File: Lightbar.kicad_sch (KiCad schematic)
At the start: 17 parts, among them IC1 PAM2863ECR, IC2 PAM2863ECR, J1 Conn_01x04_Pin

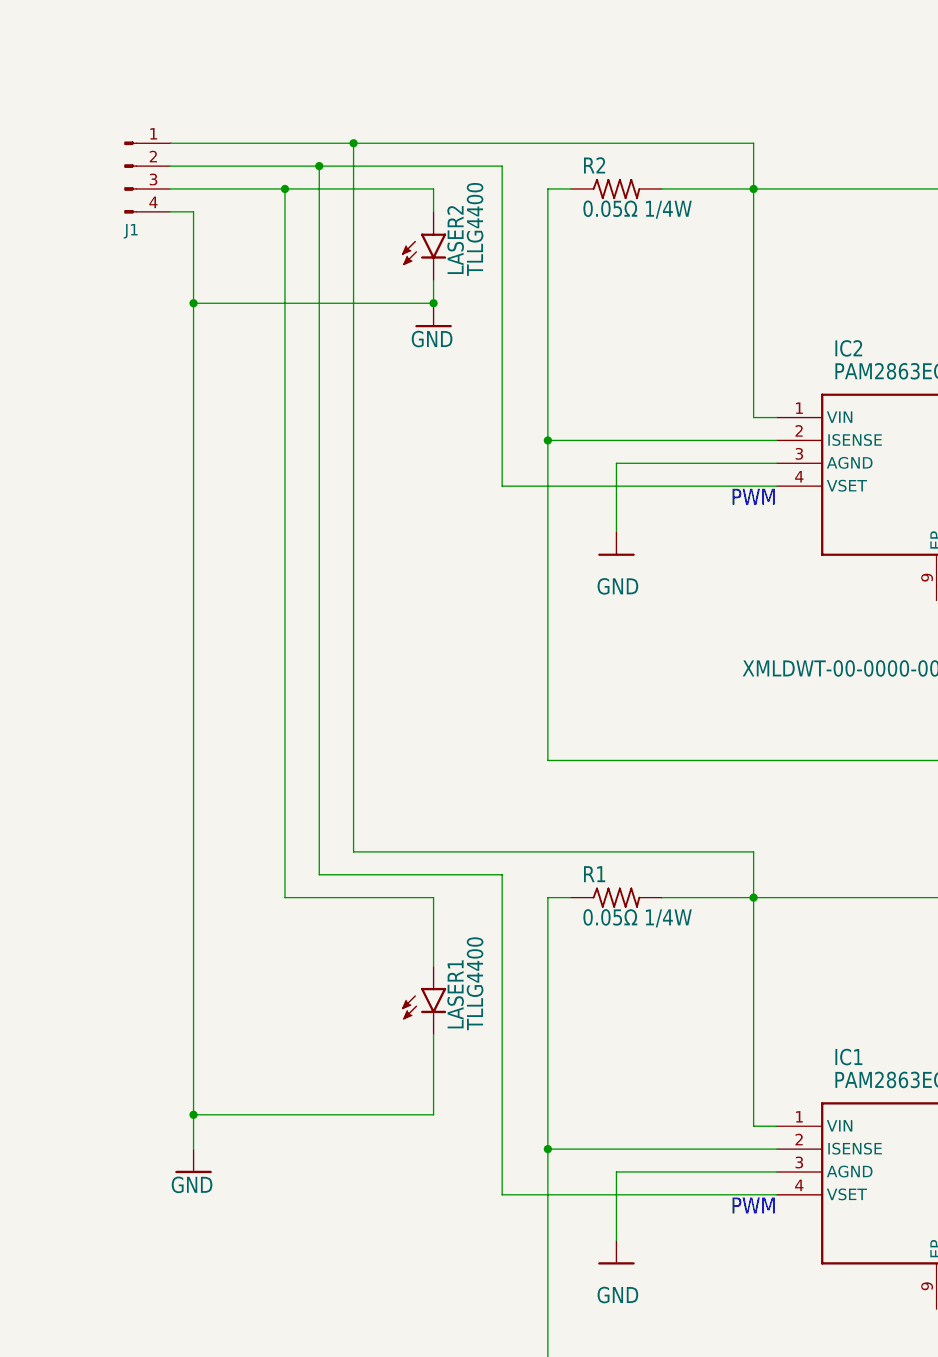
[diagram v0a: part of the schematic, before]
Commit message: updated lightbar
added resistors and transistor
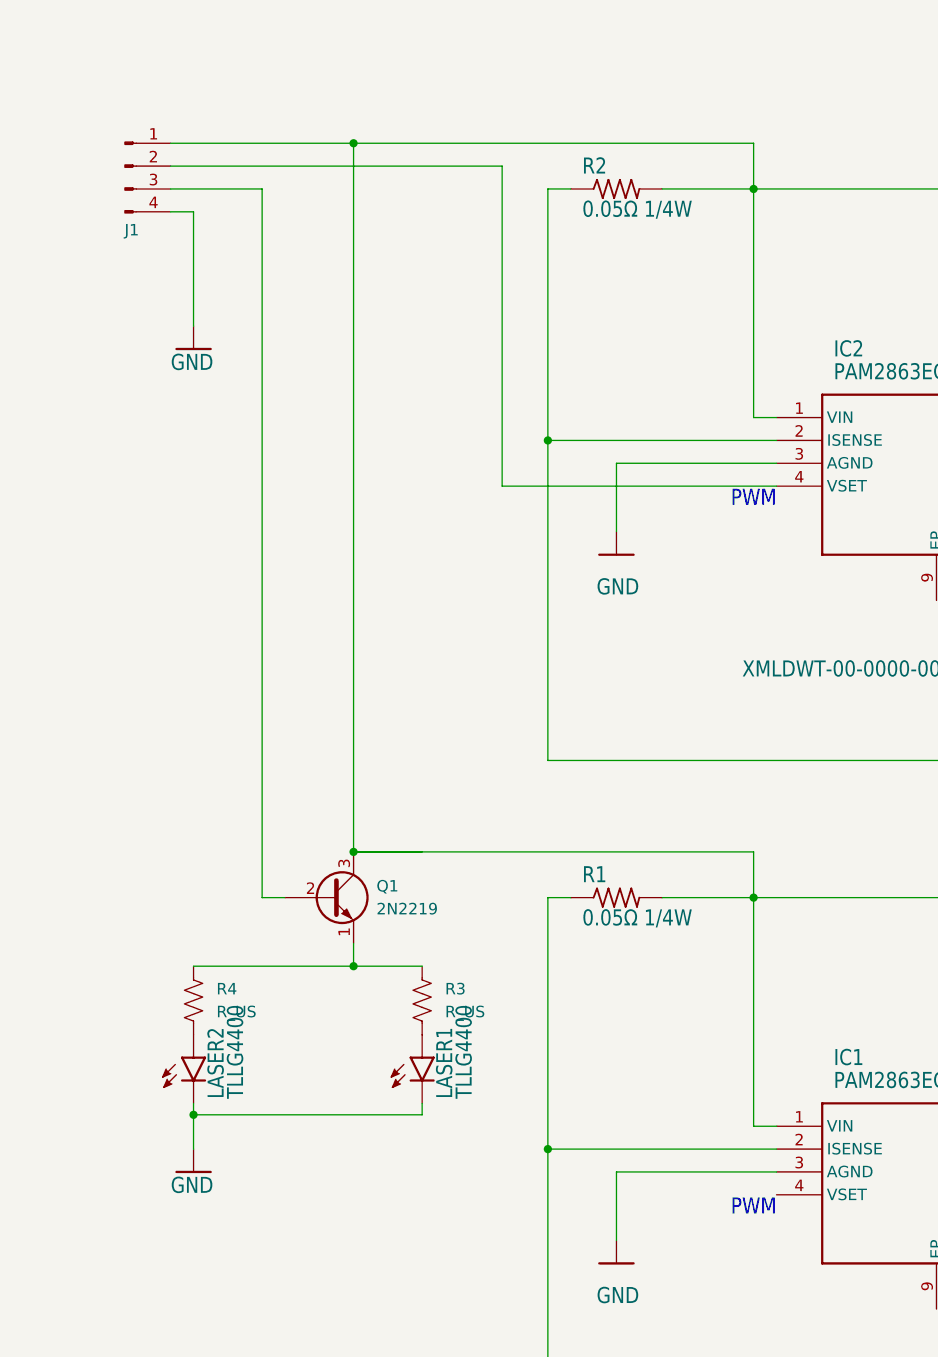
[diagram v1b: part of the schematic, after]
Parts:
- added Q1: 2N2219, Package_TO_SOT_SMD:SC-59_Handsoldering, symbol Transistor_BJT:2N2219
- added R3, R4: R_US, Resistor_SMD:R_0805_2012Metric_Pad1.20x1.40mm_HandSolder, symbol Device:R_US
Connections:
- net at C1.1, C3.1, D1.1 (K)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: now also Q1.3 (C)
- net at IC2.4 (VSET), J1.2 (Pin_2): no longer IC1.4 (VSET)
- new net: LASER2.A, R4.2
- new net: Q1.1 (E), R3.1, R4.1
- new net: J1.3 (Pin_3), Q1.2 (B)
- new net: LASER1.A, R3.2
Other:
- moved on the sheet: LASER1

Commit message: Create Final Gerber Finals
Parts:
- Q1: footprint Package_TO_SOT_SMD:SC-59_Handsoldering -> Package_TO_SOT_SMD:SOT-323_SC-70_Handsoldering
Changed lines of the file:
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@@
 			)
 		)
-		(property "Footprint" "Package_TO_SOT_SMD:SC-59_Handsoldering"
+		(property "Footprint" "Package_TO_SOT_SMD:SOT-323_SC-70_Handsoldering"
 			(at 102.87 133.985 0)
 			(effects
